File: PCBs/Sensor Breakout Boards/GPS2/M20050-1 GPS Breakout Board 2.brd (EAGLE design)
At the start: 38.1 x 43.2 mm, 7 parts, among them J1 2X6 FEMALE

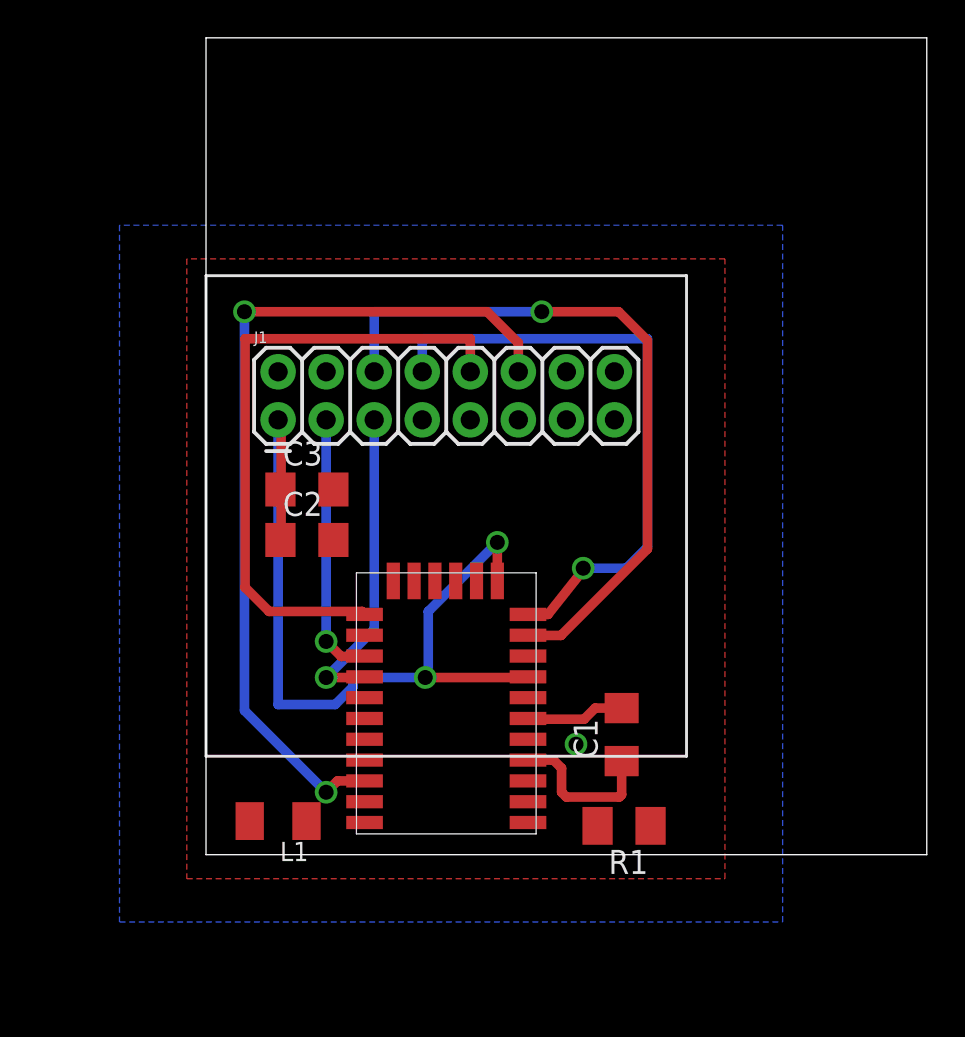
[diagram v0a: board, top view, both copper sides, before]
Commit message: GPS2 schematic
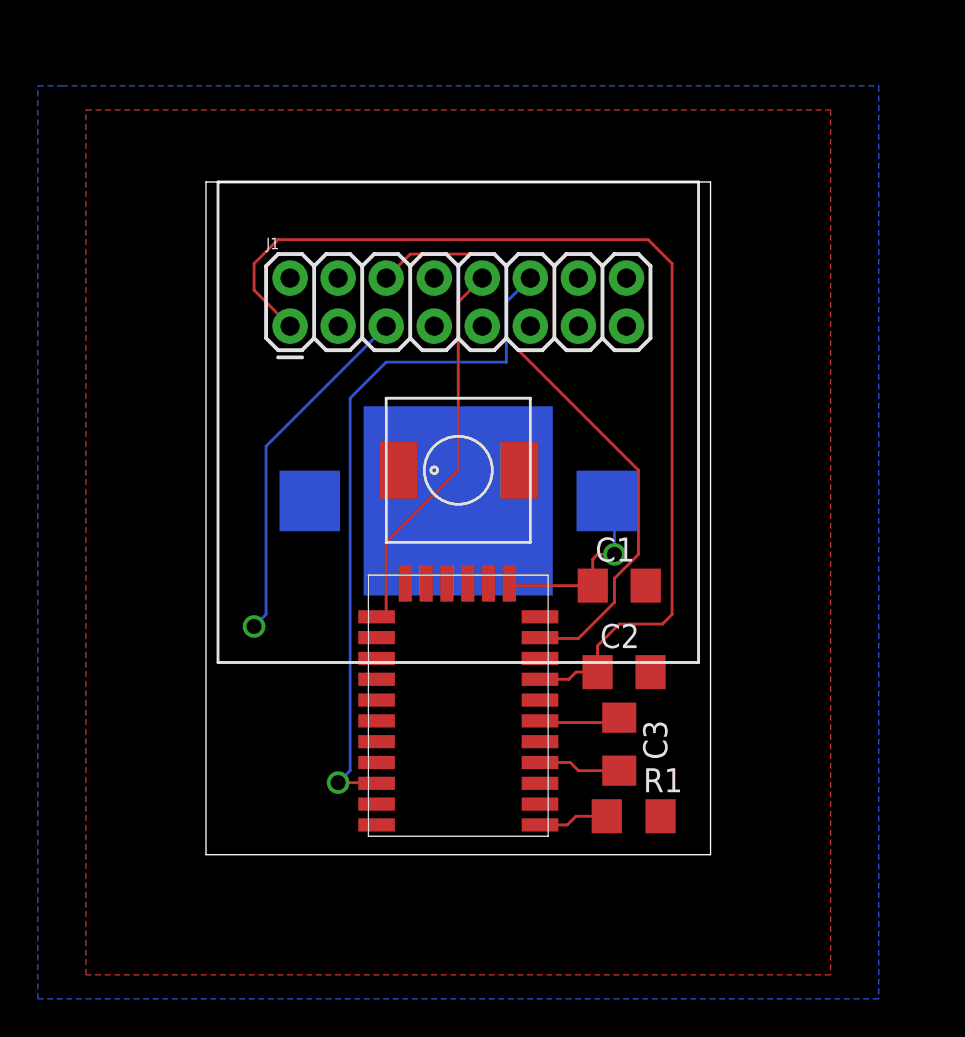
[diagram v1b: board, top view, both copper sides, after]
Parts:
- added B1: 3000K, b_keystone_3000k_sm_battery:3000K
- A1: device RTR:M20050-1_GPS -> M20050-1 GPS:M20050-1_GPS
- C1, C2: value 22 pF -> (none); device RTR:C1206 -> RTR Main Library:C1206
- C3: value 2.2 uF -> (none); device RTR:C1206 -> RTR Main Library:C1206
- J1: device RTR:2X7 -> RTR Main Library:2X7
- L1: value 1.8n -> (none); device RTR:C1206K -> RTR Main Library:L-DS75LC
- R1: value 0 -> (none); device RTR:M1206 -> RTR Main Library:R1206
- moved C3 21.3 mm to (21.8, 5.84), turned to 270 degrees
- moved L1 20.8 mm to (13.3, 20.3), turned to 0 degrees
- moved C2 18.2 mm to (22.1, 9.65)
- moved C1 7.88 mm to (21.8, 14.2), turned to 0 degrees
- moved J1 4.99 mm to (13.3, 22.9)
- moved R1 0.72 mm to (22.6, 2.03), turned to 0 degrees
- moved A1 0.65 mm to (13.3, 7.87)
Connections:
- net N$10 renamed RST
- net N$2 renamed TX
- net N$4 renamed RX
- net N$7 renamed STB
- net N$8 renamed FIX
- removed net N$11: A1.P1, R1.2
- removed net N$5: A1.P4, C1.1
- removed net N$6: A1.P6, C1.2
- removed net N$9: A1.P11, J1.8
- new net BV: A1.P12, B1.+, C1.1
- new net N$2: A1.P4, C3.2
- new net N$4: A1.P28, L1.P$1
- new net VCC: A1.P8, C2.1, J1.1
- net GND: now also B1.-, C1.2, L1.P$2, R1.2; no longer C3.2, J1.11, L1.2, R1.1
- net N$1: now also A1.P6; no longer A1.P12, A1.P8, C2.1, J1.1
- net N$3: now also A1.P1, R1.1; no longer A1.P28, L1.1
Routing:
- net VCC: track 0.00 -> 55.0 mm
- net N$1: track 46.3 -> 4.32 mm, vias 2 -> 0
- net N$9: track 32.7 -> 0.00 mm, vias 1 -> 0
- net TX: track 14.1 -> 0.00 mm, vias 1 -> 0
- net FIX: track 33.7 -> 20.4 mm
- net BV: track 0.00 -> 10.1 mm, vias 0 -> 1
- net STB: track 46.2 -> 36.6 mm, vias 2 -> 1
- net N$5: track 8.33 -> 0.00 mm
- net N$6: track 5.21 -> 0.00 mm
- net RST: track 37.5 -> 33.1 mm, vias 1 -> 0
- net N$2: track 0.00 -> 4.37 mm
- net N$3: track 0.00 -> 3.72 mm
- net RX: track 16.7 -> 18.8 mm
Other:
- board size 38.1 x 43.2 mm -> 26.7 x 35.6 mm

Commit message: first draft of gps breakout 2
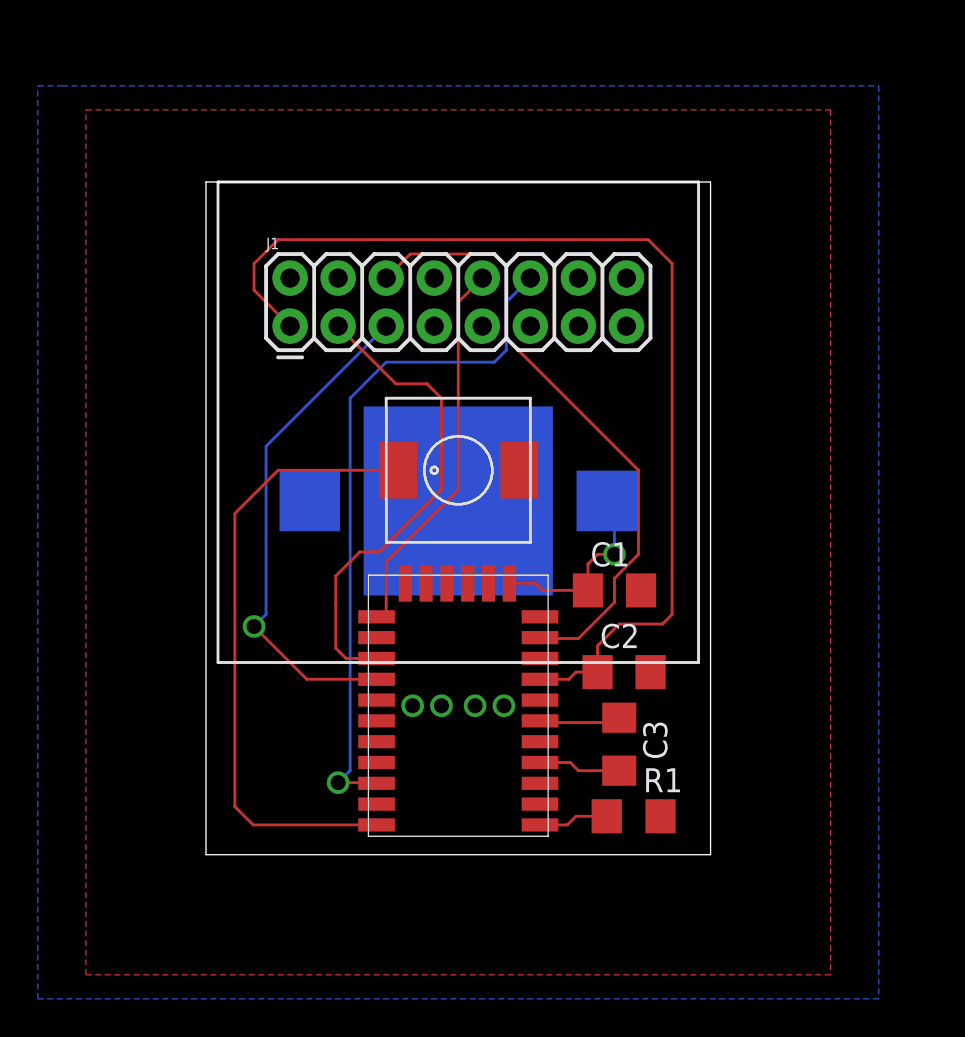
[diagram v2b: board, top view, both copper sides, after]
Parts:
- moved C1 0.36 mm to (21.6, 14.0)
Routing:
- net N$4: track 0.00 -> 33.0 mm
- net TX: track 0.00 -> 25.5 mm
- net RX: track 18.8 -> 26.4 mm
- net GND: track 0.00 -> 0.48 mm, vias 0 -> 4
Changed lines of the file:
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@@
 <?xml version="1.0" encoding="utf-8"?>
 <!DOCTYPE eagle SYSTEM "eagle.dtd">
-<eagle version="9.5.0">
+<eagle version="9.6.2">
 <drawing>
 <settings>
@@
 <attribute name="VALUE" x="3.175" y="25.527" size="0.6096" layer="27" font="vector" ratio="20"/>
 </element>
-<element name="C1" library="RTR Main Library" package="C1206" value="" x="21.844" y="14.224" smashed="yes">
-<attribute name="NAME" x="20.574" y="15.494" size="1.27" layer="25"/>
-<attribute name="VALUE" x="20.574" y="11.684" size="1.27" layer="27"/>
+<element name="C1" library="RTR Main Library" package="C1206" value="" x="21.59" y="13.97" smashed="yes">
+<attribute name="NAME" x="20.32" y="15.24" size="1.27" layer="25"/>
+<attribute name="VALUE" x="20.32" y="11.43" size="1.27" layer="27"/>
 </element>
 <element name="C2" library="RTR Main Library" package="C1206" value="" x="22.098" y="9.652" smashed="yes">
@@
 <vertex x="-8.89" y="40.64"/>
 </polygon>
-<wire x1="16.56" y1="20.32" x2="13.335" y2="18.7" width="0" layer="19" extent="1-16"/>
+<wire x1="13.335" y1="18.7" x2="13.335" y2="19.177" width="0.1524" layer="16"/>
+<via x="14.224" y="7.874" extent="1-16" drill="0.79375"/>
+<via x="15.748" y="7.874" extent="1-16" drill="0.79375"/>
+<via x="10.922" y="7.874" extent="1-16" drill="0.79375"/>
+<via x="12.446" y="7.874" extent="1-16" drill="0.79375"/>
 </signal>
 <signal name="N$1">
@@
 <wire x1="21.59" y1="18.415" x2="21.185" y2="18.7" width="0.1524" layer="16"/>
 <via x="21.59" y="15.875" extent="1-16" drill="0.79375"/>
-<wire x1="16.155" y1="14.224" x2="16.035" y2="14.344" width="0.1524" layer="1"/>
-<wire x1="20.444" y1="14.224" x2="16.155" y2="14.224" width="0.1524" layer="1"/>
-<wire x1="20.444" y1="14.224" x2="20.444" y2="15.618" width="0.1524" layer="1"/>
+<wire x1="20.19" y1="13.97" x2="20.19" y2="15.364" width="0.1524" layer="1"/>
 <wire x1="20.701" y1="15.875" x2="21.59" y2="15.875" width="0.1524" layer="1"/>
-<wire x1="20.444" y1="15.618" x2="20.701" y2="15.875" width="0.1524" layer="1"/>
+<wire x1="20.19" y1="15.364" x2="20.701" y2="15.875" width="0.1524" layer="1"/>
+<wire x1="16.035" y1="14.344" x2="17.406" y2="14.344" width="0.1524" layer="1"/>
+<wire x1="17.406" y1="14.344" x2="17.78" y2="13.97" width="0.1524" layer="1"/>
+<wire x1="17.78" y1="13.97" x2="20.19" y2="13.97" width="0.1524" layer="1"/>
 </signal>
 <signal name="N$3">
@@
 <contactref element="A1" pad="P28"/>
 <contactref element="L1" pad="P$1"/>
-<wire x1="9.015" y1="1.574" x2="10.16" y2="20.32" width="0" layer="19" extent="1-1"/>
+<wire x1="9.015" y1="1.574" x2="2.49" y2="1.574" width="0.1524" layer="1"/>
+<wire x1="2.49" y1="1.574" x2="1.524" y2="2.54" width="0.1524" layer="1"/>
+<wire x1="1.524" y1="2.54" x2="1.524" y2="18.034" width="0.1524" layer="1"/>
+<wire x1="1.524" y1="18.034" x2="3.81" y2="20.32" width="0.1524" layer="1"/>
+<wire x1="3.81" y1="20.32" x2="10.16" y2="20.32" width="0.1524" layer="1"/>
 </signal>
 <signal name="TX">
 <contactref element="A1" pad="P20"/>
 <contactref element="J1" pad="3"/>
-<wire x1="9.015" y1="10.374" x2="6.985" y2="27.94" width="0" layer="19" extent="1-1"/>
+<wire x1="6.985" y1="27.94" x2="10.033" y2="24.892" width="0.1524" layer="1"/>
+<wire x1="11.684" y1="24.892" x2="12.446" y2="24.13" width="0.1524" layer="1"/>
+<wire x1="12.446" y1="24.13" x2="12.446" y2="19.304" width="0.1524" layer="1"/>
+<wire x1="12.446" y1="19.304" x2="9.144" y2="16.002" width="0.1524" layer="1"/>
+<wire x1="9.144" y1="16.002" x2="8.128" y2="16.002" width="0.1524" layer="1"/>
+<wire x1="8.128" y1="16.002" x2="6.858" y2="14.732" width="0.1524" layer="1"/>
+<wire x1="7.406" y1="10.374" x2="9.015" y2="10.374" width="0.1524" layer="1"/>
+<wire x1="10.033" y1="24.892" x2="11.684" y2="24.892" width="0.1524" layer="1"/>
+<wire x1="6.858" y1="14.732" x2="6.858" y2="13.208" width="0.1524" layer="1"/>
+<wire x1="6.858" y1="13.208" x2="6.858" y2="10.922" width="0.1524" layer="1"/>
+<wire x1="6.858" y1="10.922" x2="7.406" y2="10.374" width="0.1524" layer="1"/>
 </signal>
 <signal name="RX">
@@
 <wire x1="9.525" y1="27.94" x2="3.175" y2="21.59" width="0.1524" layer="16"/>
 <via x="2.54" y="12.065" extent="1-16" drill="0.79375"/>
-<wire x1="9.015" y1="9.274" x2="2.54" y2="12.065" width="0" layer="19" extent="1-1"/>
+<wire x1="9.015" y1="9.274" x2="5.331" y2="9.274" width="0.1524" layer="1"/>
+<wire x1="5.331" y1="9.274" x2="2.54" y2="12.065" width="0.1524" layer="1"/>
 </signal>
 <signal name="RST">
@@
 <contactref element="J1" pad="10"/>
 <contactref element="A1" pad="P18"/>
-<wire x1="9.525" y1="16.51" x2="9.525" y2="12.7" width="0.1524" layer="1"/>
-<wire x1="13.335" y1="20.32" x2="9.525" y2="16.51" width="0.1524" layer="1"/>
-<wire x1="13.335" y1="29.21" x2="13.335" y2="20.32" width="0.1524" layer="1"/>
+<wire x1="9.525" y1="15.494" x2="9.525" y2="12.7" width="0.1524" layer="1"/>
+<wire x1="13.335" y1="19.304" x2="9.525" y2="15.494" width="0.1524" layer="1"/>
+<wire x1="13.335" y1="29.21" x2="13.335" y2="19.304" width="0.1524" layer="1"/>
 <wire x1="14.605" y1="30.48" x2="13.335" y2="29.21" width="0.1524" layer="1"/>
 <wire x1="9.525" y1="12.7" x2="9.015" y2="12.574" width="0.1524" layer="1"/>
@@
 <wire x1="7.62" y1="4.445" x2="6.985" y2="3.81" width="0.1524" layer="16"/>
 <wire x1="7.62" y1="24.13" x2="7.62" y2="4.445" width="0.1524" layer="16"/>
-<wire x1="9.525" y1="26.035" x2="7.62" y2="24.13" width="0.1524" layer="16"/>
-<wire x1="15.875" y1="26.035" x2="9.525" y2="26.035" width="0.1524" layer="16"/>
-<wire x1="15.875" y1="29.21" x2="15.875" y2="26.035" width="0.1524" layer="16"/>
+<wire x1="7.62" y1="24.13" x2="9.525" y2="26.035" width="0.1524" layer="16"/>
+<wire x1="15.875" y1="26.67" x2="15.875" y2="29.21" width="0.1524" layer="16"/>
 <wire x1="17.145" y1="30.48" x2="15.875" y2="29.21" width="0.1524" layer="16"/>
 <wire x1="8.89" y1="3.81" x2="9.015" y2="3.774" width="0.1524" layer="1"/>
 <via x="6.985" y="3.81" extent="1-16" drill="0.79375"/>
+<wire x1="15.24" y1="26.035" x2="15.875" y2="26.67" width="0.1524" layer="16"/>
+<wire x1="9.525" y1="26.035" x2="15.24" y2="26.035" width="0.1524" layer="16"/>
 </signal>
 </signals>

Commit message: finish gpsv2
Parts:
- C1, C3: value (none) -> 22p
- C2: value (none) -> 2.2u
- L1: value (none) -> 1.8n
- R1: value (none) -> 0R
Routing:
- net GND: vias 4 -> 6
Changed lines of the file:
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@@
 <setting verticaltext="up"/>
 </settings>
-<grid distance="10" unitdist="mil" unit="mil" style="lines" multiple="1" display="no" altdistance="5" altunitdist="mil" altunit="mil"/>
+<grid distance="10" unitdist="mil" unit="mil" style="lines" multiple="1" display="no" altdistance="10" altunitdist="mil" altunit="mil"/>
 <layers>
 <layer number="1" name="Top" color="4" fill="1" visible="yes" active="yes"/>
@@
 <attribute name="VALUE" x="3.175" y="25.527" size="0.6096" layer="27" font="vector" ratio="20"/>
 </element>
-<element name="C1" library="RTR Main Library" package="C1206" value="" x="21.59" y="13.97" smashed="yes">
+<element name="C1" library="RTR Main Library" package="C1206" value="22p" x="21.59" y="13.97" smashed="yes">
 <attribute name="NAME" x="20.32" y="15.24" size="1.27" layer="25"/>
 <attribute name="VALUE" x="20.32" y="11.43" size="1.27" layer="27"/>
 </element>
-<element name="C2" library="RTR Main Library" package="C1206" value="" x="22.098" y="9.652" smashed="yes">
+<element name="C2" library="RTR Main Library" package="C1206" value="2.2u" x="22.098" y="9.652" smashed="yes">
 <attribute name="NAME" x="20.828" y="10.922" size="1.27" layer="25"/>
 <attribute name="VALUE" x="20.828" y="7.112" size="1.27" layer="27"/>
 </element>
-<element name="C3" library="RTR Main Library" package="C1206" value="" x="21.844" y="5.842" smashed="yes" rot="R270">
+<element name="C3" library="RTR Main Library" package="C1206" value="22p" x="21.844" y="5.842" smashed="yes" rot="R270">
 <attribute name="NAME" x="23.114" y="7.112" size="1.27" layer="25" rot="R270"/>
 <attribute name="VALUE" x="19.304" y="7.112" size="1.27" layer="27" rot="R270"/>
 </element>
-<element name="R1" library="RTR Main Library" package="R1206" value="" x="22.606" y="2.032" smashed="yes">
+<element name="R1" library="RTR Main Library" package="R1206" value="0R" x="22.606" y="2.032" smashed="yes">
 <attribute name="NAME" x="23.114" y="3.302" size="1.27" layer="25"/>
 <attribute name="VALUE" x="21.336" y="-0.508" size="1.27" layer="27"/>
 </element>
-<element name="L1" library="RTR Main Library" package="L-DS75LC" value="" x="13.335" y="20.32" smashed="yes"/>
+<element name="L1" library="RTR Main Library" package="L-DS75LC" value="1.8n" x="13.335" y="20.32" smashed="yes"/>
 </elements>
 <signals>
@@
 <via x="10.922" y="7.874" extent="1-16" drill="0.79375"/>
 <via x="12.446" y="7.874" extent="1-16" drill="0.79375"/>
+<via x="11.176" y="12.192" extent="1-16" drill="0.79375"/>
+<via x="6.604" y="6.604" extent="1-16" drill="0.79375"/>
 </signal>
 <signal name="N$1">
@@
 <contactref element="J1" pad="10"/>
 <contactref element="A1" pad="P18"/>
-<wire x1="9.525" y1="15.494" x2="9.525" y2="12.7" width="0.1524" layer="1"/>
-<wire x1="13.335" y1="19.304" x2="9.525" y2="15.494" width="0.1524" layer="1"/>
 <wire x1="13.335" y1="29.21" x2="13.335" y2="19.304" width="0.1524" layer="1"/>
 <wire x1="14.605" y1="30.48" x2="13.335" y2="29.21" width="0.1524" layer="1"/>
-<wire x1="9.525" y1="12.7" x2="9.015" y2="12.574" width="0.1524" layer="1"/>
+<wire x1="9.015" y1="14.984" x2="9.015" y2="12.574" width="0.1524" layer="1"/>
+<wire x1="13.335" y1="19.304" x2="9.015" y2="14.984" width="0.1524" layer="1"/>
 </signal>
 <signal name="STB">
